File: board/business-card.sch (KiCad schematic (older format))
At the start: 41 parts

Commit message: add footprints and start schematic (still need connector footprint)
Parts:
- removed SW?: SW_SPST, symbol Switch:SW_SPST
- added SW1: PTS_540, C_K:PTS_540, symbol C_K:PTS_540
- BT1: renamed from BT?; footprint (none) -> renata:CR1216_MFR_SM
- C1, C2, C3: renamed from C?; footprint (none) -> Capacitor_SMD:C_0603_1608Metric
- D1, D10, D11, D12, D13, D14, D15, D16, D2, D3, D4, D5, D6, D7, D8, D9: renamed from D?; footprint (none) -> LED_SMD:LED_0603_1608Metric
- R1, R10, R11, R12, R13, R14, R15, R16, R17, R2, R3, R4, R5, R6, R7, R8, R9: renamed from R?; footprint (none) -> Resistor_SMD:R_0603_1608Metric
- U2: renamed from U?; footprint (none) -> Package_LGA:LGA-12_2x2mm_P0.5mm
- gave numbers to parts that had none: 2
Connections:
- wire segments 86 -> 94

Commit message: Changed mcu to attiny (for cap touch), removed led resistors (not going to need them), changed switch symbol.
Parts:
- removed C3: 0.1 uF, Capacitor_SMD:C_0603_1608Metric, symbol Device:C
- removed J1: Conn_01x04, symbol Connector_Generic:Conn_01x04
- removed R1: 10 K, Resistor_SMD:R_0603_1608Metric, symbol Device:R
- removed R10, R11, R12, R13, R14, R15, R16, R17, R2, R3, R4, R5, R6, R7, R8, R9: 600, Resistor_SMD:R_0603_1608Metric, symbol Device:R
- removed SW1: PTS_540, C_K:PTS_540, symbol C_K:PTS_540
- removed U1: STM8S003F3U, Package_DFN_QFN:ST_UFQFPN-20_3x3mm_P0.5mm, symbol MCU_ST_STM8:STM8S003F3U
- removed U2: KX003-1077, Package_LGA:LGA-12_2x2mm_P0.5mm, symbol kionix:KX003-1077
- added C?: 0.1 uF, Capacitor_SMD:C_0603_1608Metric, symbol Device:C
- added J?: Conn_01x10, symbol Connector_Generic:Conn_01x10
- added R? (x2): R, symbol Device:R
- added SW?: SW_SPST, symbol Switch:SW_SPST
- added U?: ATtiny1616-S, Package_SO:SOIC-20W_7.5x12.8mm_P1.27mm, symbol MCU_Microchip_ATtiny:ATtiny1616-S
- C1: value 0.1 uF -> 1 uF
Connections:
- net labels added: SWCLK, SWDIO, nRESET
- net labels removed: NRESET, SCL, SDA, SWIM
- wire segments 94 -> 62
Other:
- moved on the sheet: C1, C2

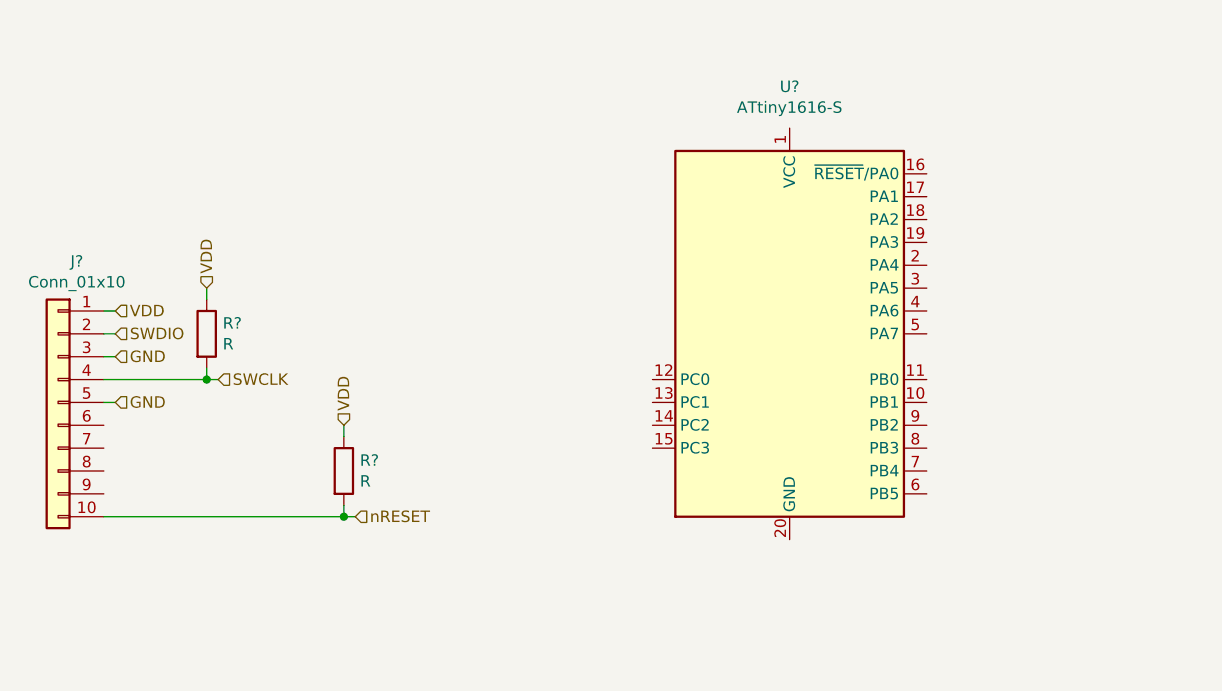
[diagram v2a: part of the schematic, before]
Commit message: Changed programming connector to updi pinout.
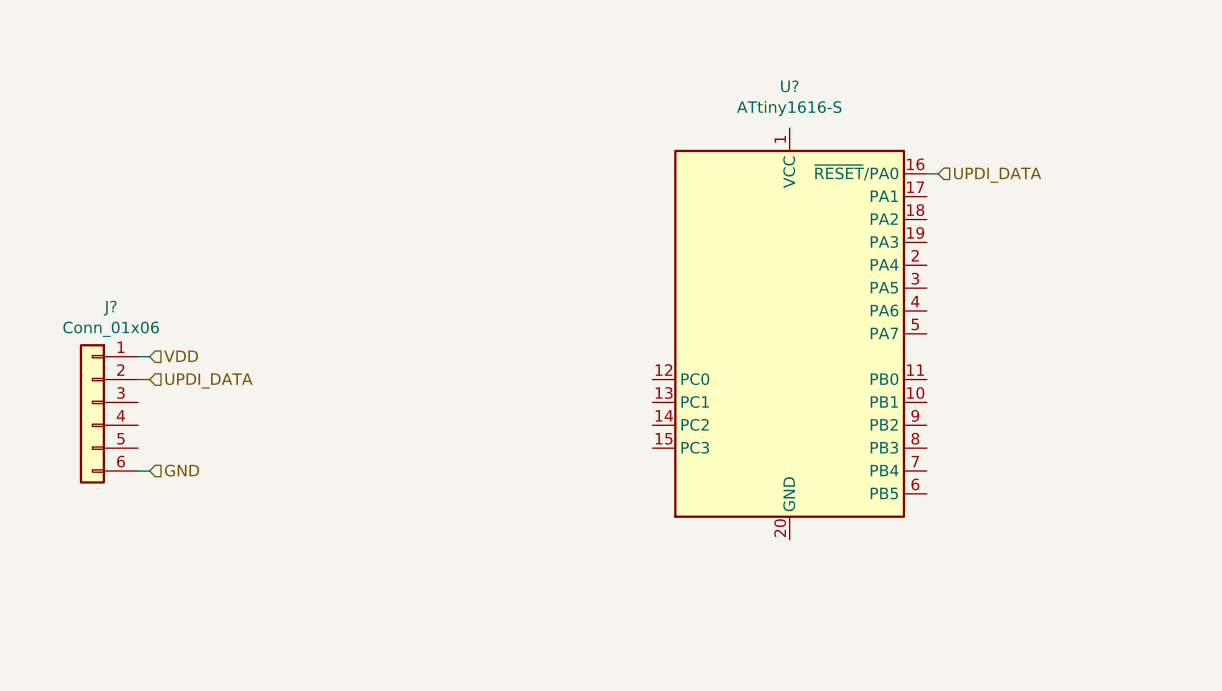
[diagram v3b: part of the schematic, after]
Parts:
- removed J?: Conn_01x10, symbol Connector_Generic:Conn_01x10
- removed R? (x2): R, symbol Device:R
- added J?: Conn_01x06, symbol Connector_Generic:Conn_01x06
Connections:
- net labels added: UPDI_DATA
- wire segments 62 -> 54
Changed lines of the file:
@@
 Wire Wire Line
 	4350 6700 4350 6650
-$Comp
-L Connector_Generic:Conn_01x10 J?
-U 1 1 60929001
-P 1050 4750
-F 0 "J?" H 968 5367 50  0000 C CNN
-F 1 "Conn_01x10" H 968 5276 50  0000 C CNN
-F 2 "" H 1050 4750 50  0001 C CNN
-F 3 "~" H 1050 4750 50  0001 C CNN
-	1    1050 4750
-	-1   0    0    -1
-$EndComp
 Wire Wire Line
 	4000 2750 4050 2750
@@
 	4650 2850 4650 2550
 Connection ~ 4650 2550
-Text HLabel 1300 4350 2    50   Input ~ 0
-VDD
-Wire Wire Line
-	1300 4350 1250 4350
-Text HLabel 1300 4450 2    50   Input ~ 0
-SWDIO
-Text HLabel 1300 4550 2    50   Input ~ 0
-GND
-Text HLabel 1750 4650 2    50   Input ~ 0
-SWCLK
-Text HLabel 1300 4750 2    50   Input ~ 0
-GND
-Text HLabel 2350 5250 2    50   Input ~ 0
-nRESET
-Wire Wire Line
-	2350 5250 2300 5250
-Wire Wire Line
-	1250 4750 1300 4750
-Wire Wire Line
-	1250 4550 1300 4550
-Wire Wire Line
-	1300 4450 1250 4450
-Wire Wire Line
-	1250 4650 1700 4650
-$Comp
-L Device:R R?
-U 1 1 60946BA4
-P 1700 4450
-F 0 "R?" H 1770 4496 50  0000 L CNN
-F 1 "R" H 1770 4405 50  0000 L CNN
-F 2 "" V 1630 4450 50  0001 C CNN
-F 3 "~" H 1700 4450 50  0001 C CNN
-	1    1700 4450
-	1    0    0    -1
-$EndComp
-Wire Wire Line
-	1700 4600 1700 4650
-Connection ~ 1700 4650
-Wire Wire Line
-	1700 4650 1750 4650
-Wire Wire Line
-	1700 4300 1700 4250
-Text HLabel 1700 4250 1    50   Input ~ 0
-VDD
-$Comp
-L Device:R R?
-U 1 1 60949E52
-P 2300 5050
-F 0 "R?" H 2370 5096 50  0000 L CNN
-F 1 "R" H 2370 5005 50  0000 L CNN
-F 2 "" V 2230 5050 50  0001 C CNN
-F 3 "~" H 2300 5050 50  0001 C CNN
-	1    2300 5050
-	1    0    0    -1
-$EndComp
-Wire Wire Line
-	2300 4900 2300 4850
-Text HLabel 2300 4850 1    50   Input ~ 0
-VDD
-Wire Wire Line
-	2300 5200 2300 5250
-Connection ~ 2300 5250
-Wire Wire Line
-	1250 5250 2300 5250
 Text HLabel 3600 6450 0    50   Input ~ 0
 nRESET
@@
 	1    0    0    -1
 $EndComp
+$Comp
+L Connector_Generic:Conn_01x06 J?
+U 1 1 6092ADDC
+P 1200 4750
+F 0 "J?" H 1118 5167 50  0000 C CNN
+F 1 "Conn_01x06" H 1118 5076 50  0000 C CNN
+F 2 "" H 1200 4750 50  0001 C CNN
+F 3 "~" H 1200 4750 50  0001 C CNN
+	1    1200 4750
+	-1   0    0    -1
+$EndComp
+Wire Wire Line
+	1450 4650 1400 4650
+Text HLabel 1450 4650 2    50   Input ~ 0
+UPDI_DATA
+Text HLabel 1450 4550 2    50   Input ~ 0
+VDD
+Wire Wire Line
+	1450 4550 1400 4550
+Wire Wire Line
+	1450 5050 1400 5050
+Text HLabel 1450 5050 2    50   Input ~ 0
+GND
+Wire Wire Line
+	4900 3750 4850 3750
+Text HLabel 4900 3750 2    50   Input ~ 0
+UPDI_DATA
 $EndSCHEMATC

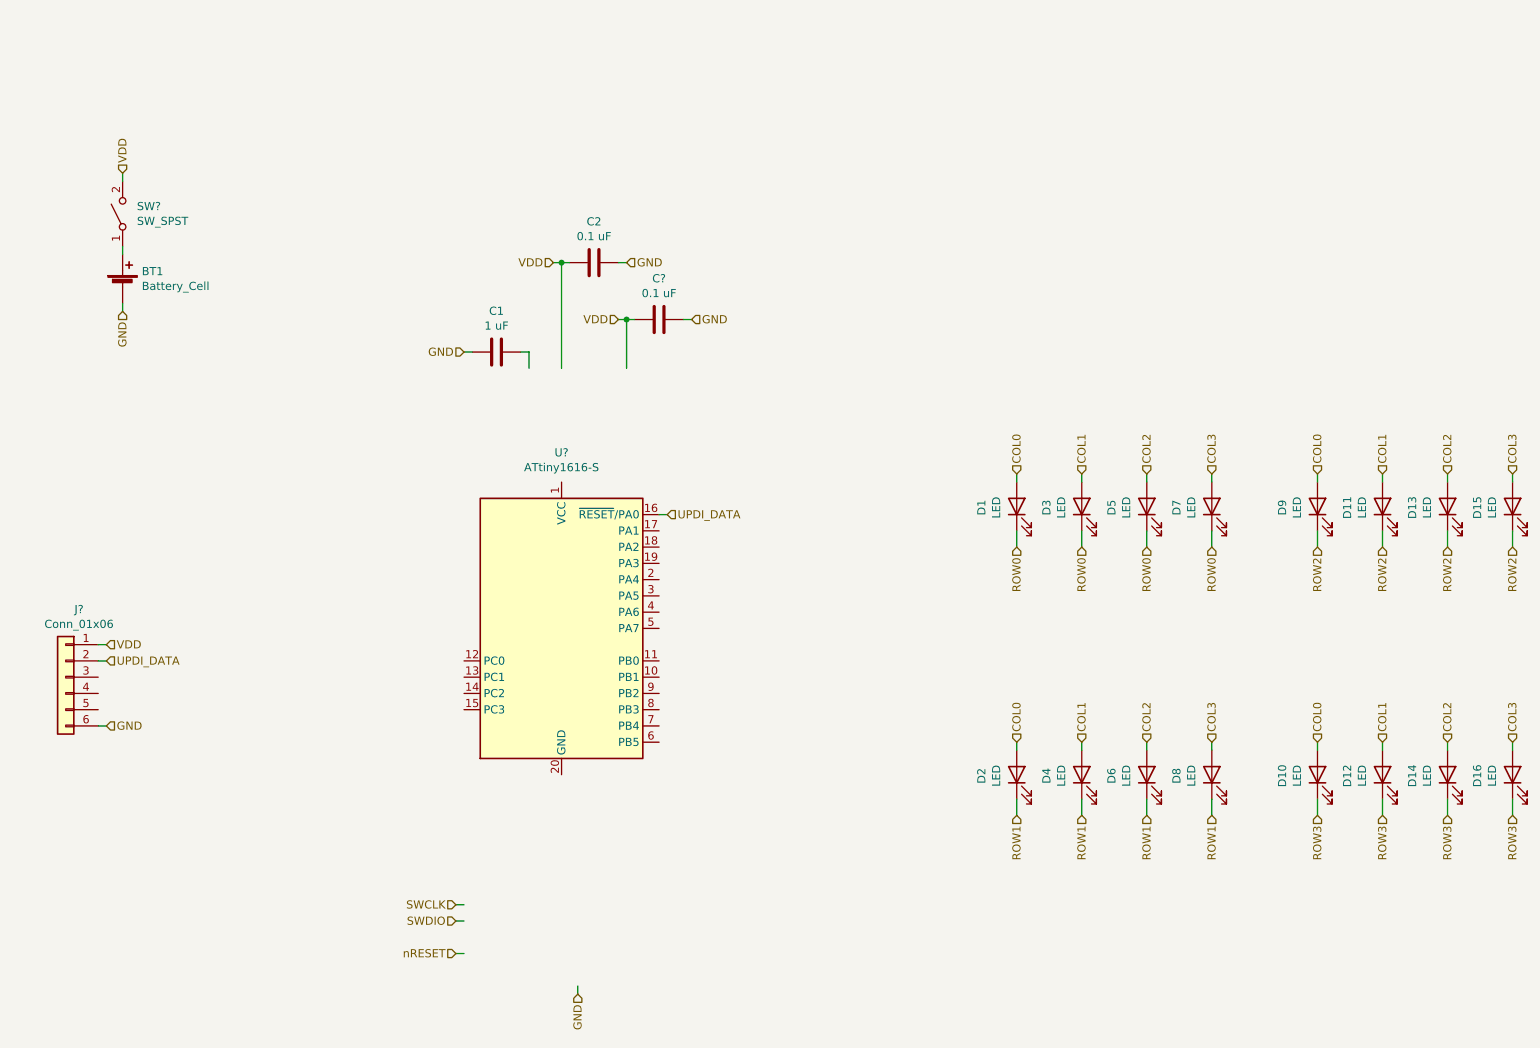
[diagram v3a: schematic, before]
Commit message: Added another row and column of leds, and buttons.
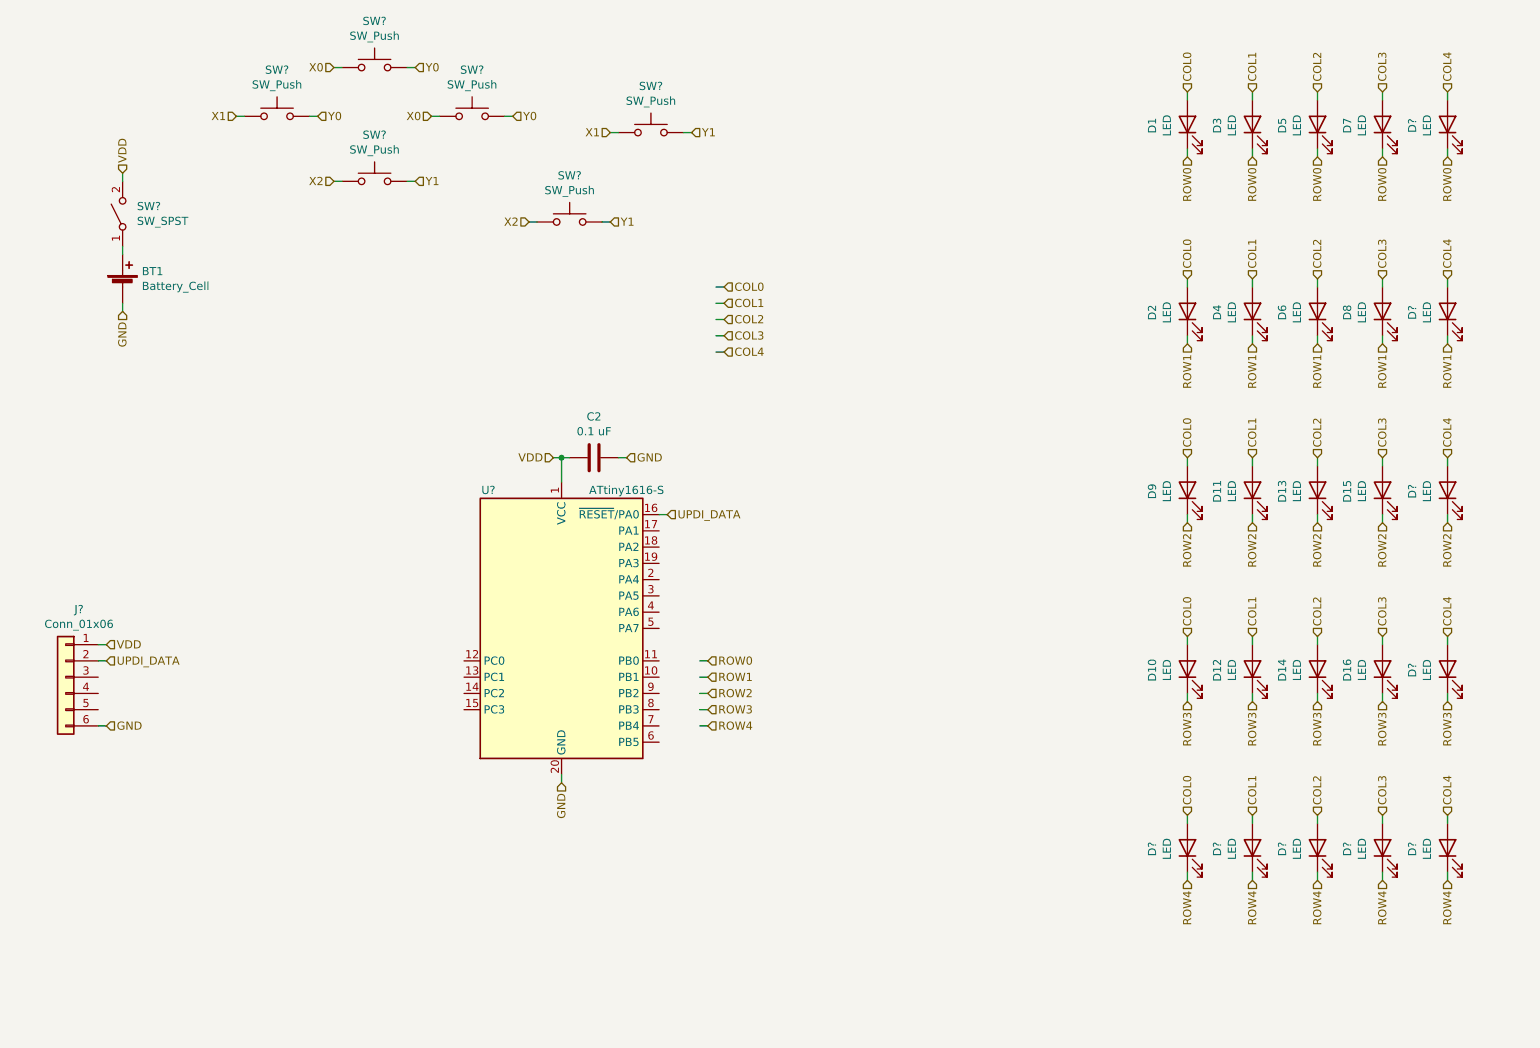
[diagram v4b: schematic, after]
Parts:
- removed C1: 1 uF, Capacitor_SMD:C_0603_1608Metric, symbol Device:C
- removed C?: 0.1 uF, Capacitor_SMD:C_0603_1608Metric, symbol Device:C
- added D? (x9): LED, LED_SMD:LED_0603_1608Metric, symbol Device:LED
- added SW? (x6): SW_Push, symbol Switch:SW_Push
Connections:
- net labels added: COL4, ROW4, X0, X1, X2, Y0, Y1
- net labels removed: SWCLK, SWDIO, nRESET
- wire segments 54 -> 84
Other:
- moved on the sheet: C2, D1, D10, D11, D12, D13, D14, D15, D16, D2, D3, D4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

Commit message: Annotated board, added some part numbers and footprints.
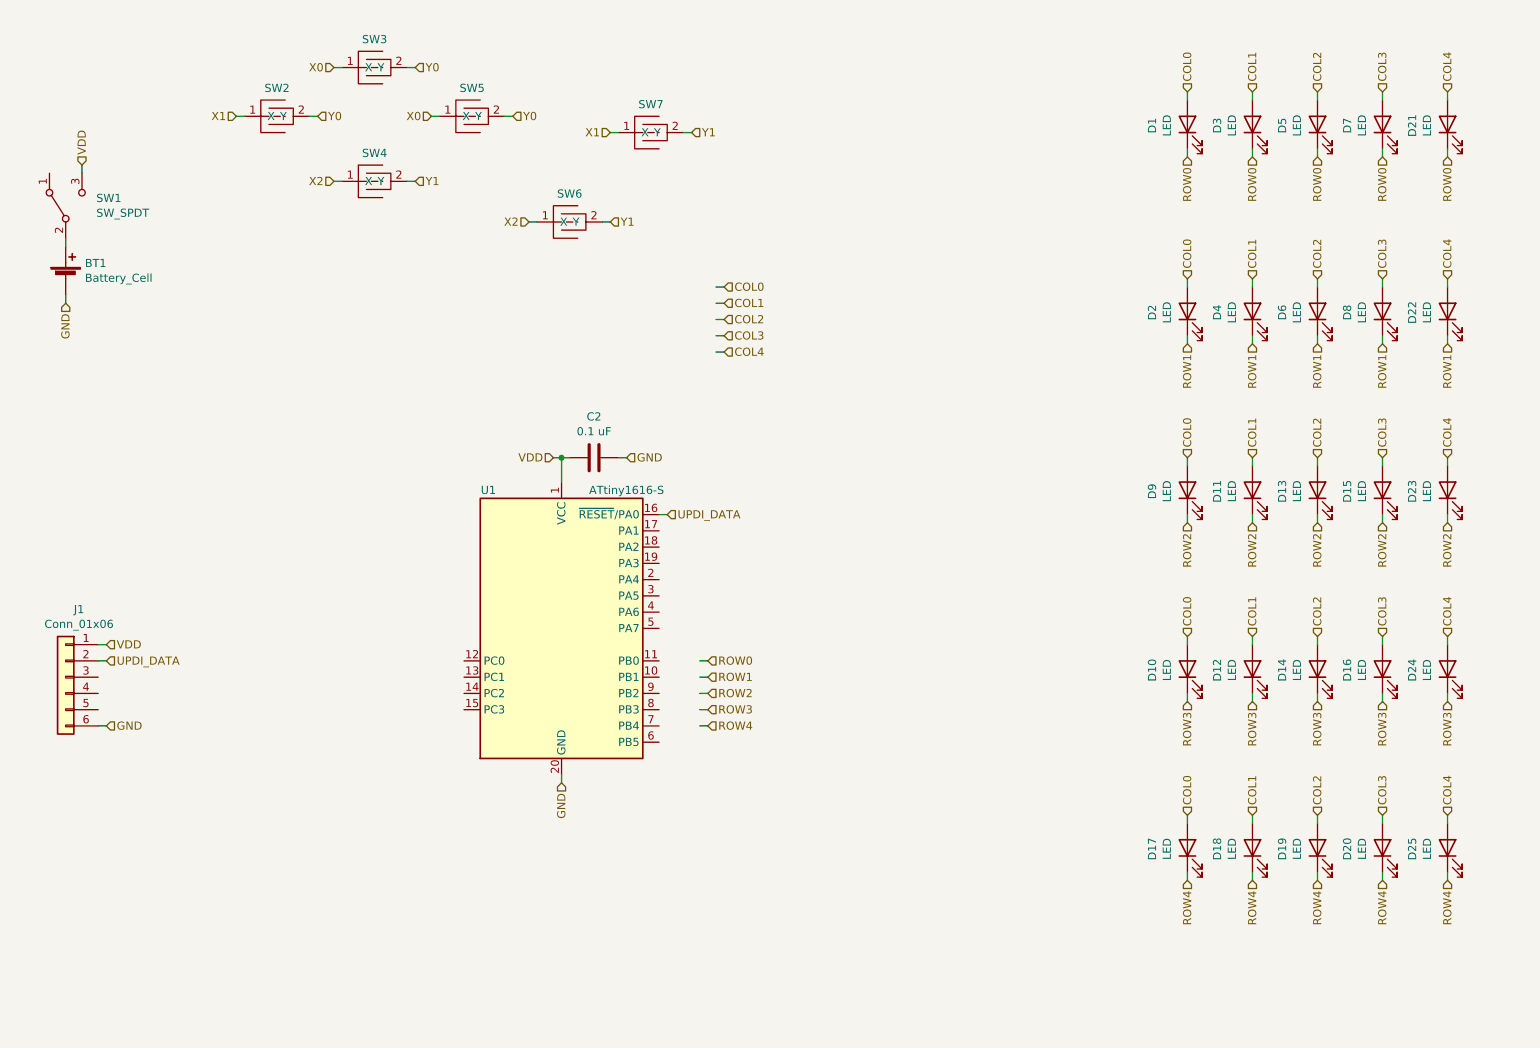
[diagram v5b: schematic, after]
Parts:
- removed SW?: SW_SPST, symbol Switch:SW_SPST
- removed SW? (x6): SW_Push, symbol Switch:SW_Push
- added SW1: SW_SPDT, colinholzman:JSX08001SAQNL-through-board-mount, symbol Switch:SW_SPDT
- added SW2, SW3, SW4, SW5, SW6, SW7: Mutual_Capacitance_Button, colinholzman:Mutual_Capacitance_Button, symbol colinholzman:Mutual_Capacitance_Button
- D1, D10, D11, D12, D13, D14, D15, D16, D2, D3, D4, D5, D6, D7, D8, D9: mfg1 (none) -> SunLED; mfg1pn (none) -> XZCBD53W-6
- D17, D18, D19, D20, D21, D22, D23, D24, D25: renamed from D?; mfg1 (none) -> SunLED; mfg1pn (none) -> XZCBD53W-6
- gave numbers to parts that had none: 2
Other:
- moved on the sheet: BT1

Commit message: Added footprint for programming connector and added programming adapter board project.
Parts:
- J1: footprint (none) -> colinholzman:Molex_788641001_mating_pad_layout; exclude (none) -> yes
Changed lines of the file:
@@
 F 0 "J1" H 1118 5167 50  0000 C CNN
 F 1 "Conn_01x06" H 1118 5076 50  0000 C CNN
-F 2 "" H 1200 4750 50  0001 C CNN
+F 2 "colinholzman:Molex_788641001_mating_pad_layout" H 1200 4750 50  0001 C CNN
 F 3 "~" H 1200 4750 50  0001 C CNN
+F 4 "yes" H 1200 4750 50  0001 C CNN "exclude"
 	1    1200 4750
 	-1   0    0    -1
